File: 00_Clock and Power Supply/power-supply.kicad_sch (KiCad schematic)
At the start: 9 parts, among them J3 Jack-DC, Q1 TIP126, SW1 SPST, U1 L7805

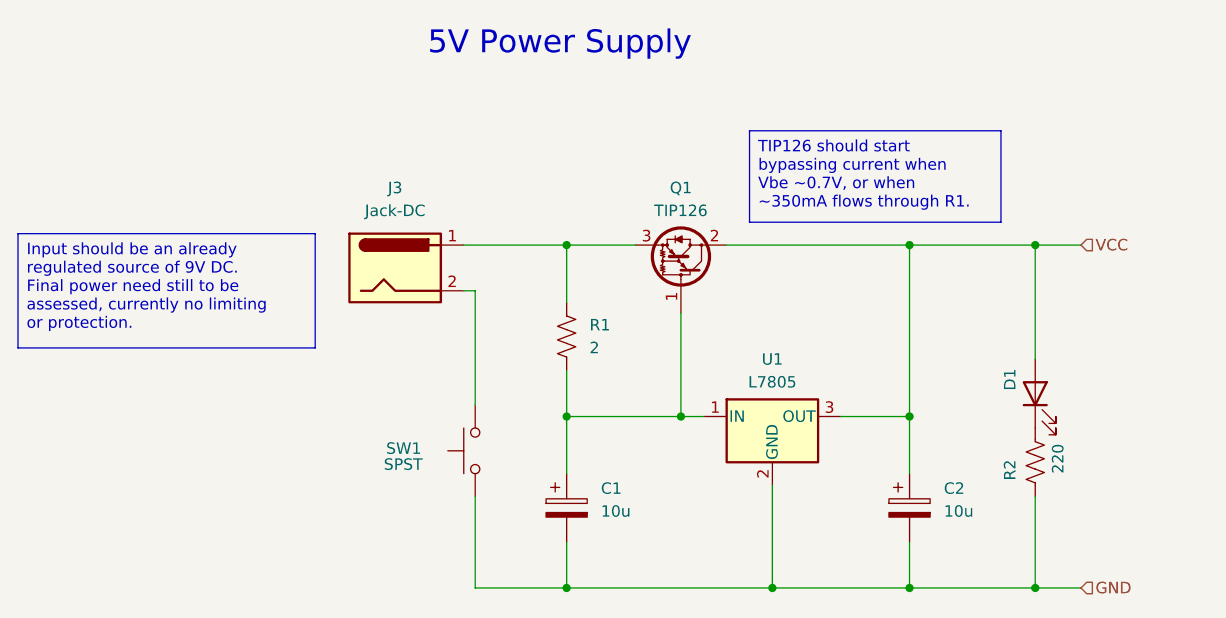
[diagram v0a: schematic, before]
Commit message: Last revision of the cpu, all boards have been ordered. Implementation to be tested and documented in following commits.
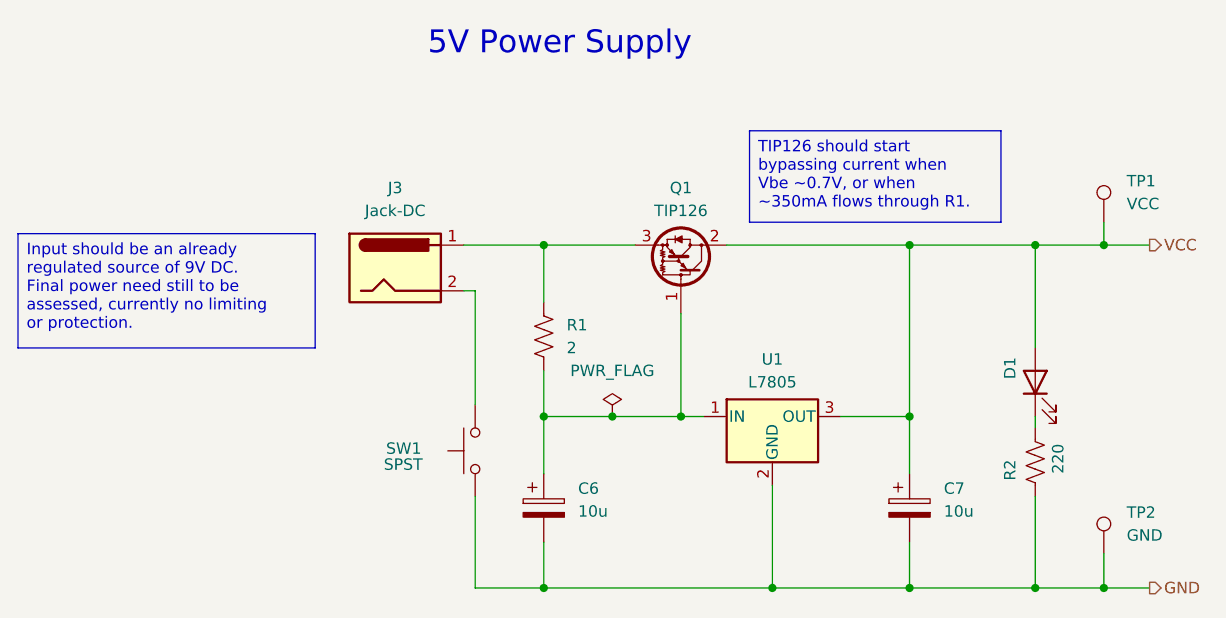
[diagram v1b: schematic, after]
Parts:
- added TP1: VCC, TestPoint:TestPoint_Loop_D3.50mm_Drill0.9mm_Beaded, symbol Connector:TestPoint
- added TP2: GND, TestPoint:TestPoint_Loop_D3.50mm_Drill0.9mm_Beaded, symbol Connector:TestPoint
- renumbered C1 to C6, C2 to C7
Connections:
- net GND: now also TP2.1
- net VCC: now also TP1.1
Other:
- moved on the sheet: C6, D1, R1
